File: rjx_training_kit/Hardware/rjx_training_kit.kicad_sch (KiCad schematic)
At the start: 20 parts, among them J1 Barrel_Jack_Switch, J2 Conn_01x32_Pin, J3 Conn_01x32_Pin, Q1 BC817, U1 TLV76133DCY, U2 LD39200DPUR

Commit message: [RJX]: Initial footprint assignment. This is subject to further review and analysis.
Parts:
- C1, C2, C3, C4: footprint (none) -> Capacitor_SMD:C_0603_1608Metric
- D1: footprint (none) -> LED_SMD:LED_0603_1608Metric
- H1, H2, H3, H4: footprint (none) -> MountingHole:MountingHole_3mm
- J1: footprint (none) -> Connector_BarrelJack:BarrelJack_Horizontal
- J2, J3: footprint (none) -> Connector_PinHeader_2.54mm:PinHeader_1x32_P2.54mm_Vertical
- R1, R2, R3, R4, R5: footprint (none) -> Resistor_SMD:R_0603_1608Metric
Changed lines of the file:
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@@
 			)
 		)
-		(property "Footprint" ""
+		(property "Footprint" "Resistor_SMD:R_0603_1608Metric"
 			(at 47.244 171.704 90)
 			(effects
@@
 			)
 		)
-		(property "Footprint" ""
+		(property "Footprint" "Capacitor_SMD:C_0603_1608Metric"
 			(at 132.3848 53.34 0)
 			(effects
@@
 			)
 		)
-		(property "Footprint" ""
+		(property "Footprint" "MountingHole:MountingHole_3mm"
 			(at 125.73 177.8 0)
 			(effects
@@
 			)
 		)
-		(property "Footprint" ""
+		(property "Footprint" "Connector_BarrelJack:BarrelJack_Horizontal"
 			(at 46.99 41.656 0)
 			(effects
@@
 			)
 		)
-		(property "Footprint" ""
+		(property "Footprint" "Resistor_SMD:R_0603_1608Metric"
 			(at 61.976 153.924 90)
 			(effects
@@
 			)
 		)
-		(property "Footprint" ""
+		(property "Footprint" "Capacitor_SMD:C_0603_1608Metric"
 			(at 35.8648 104.14 0)
 			(effects
@@
 			)
 		)
-		(property "Footprint" ""
+		(property "Footprint" "Connector_PinHeader_2.54mm:PinHeader_1x32_P2.54mm_Vertical"
 			(at 124.46 119.38 0)
 			(effects
@@
 			)
 		)
-		(property "Footprint" ""
+		(property "Footprint" "MountingHole:MountingHole_3mm"
 			(at 101.6 177.8 0)
 			(effects
@@
 			)
 		)
-		(property "Footprint" ""
+		(property "Footprint" "LED_SMD:LED_0603_1608Metric"
 			(at 60.96 162.56 0)
 			(effects
@@
 			)
 		)
-		(property "Footprint" ""
+		(property "Footprint" "Resistor_SMD:R_0603_1608Metric"
 			(at 41.656 158.496 90)
 			(effects
@@
 			)
 		)
-		(property "Footprint" ""
+		(property "Footprint" "Resistor_SMD:R_0603_1608Metric"
 			(at 144.526 32.766 90)
 			(effects
@@
 			)
 		)
-		(property "Footprint" ""
+		(property "Footprint" "Resistor_SMD:R_0603_1608Metric"
 			(at 144.526 49.276 90)
 			(effects
@@
 			)
 		)
-		(property "Footprint" ""
+		(property "Footprint" "MountingHole:MountingHole_3mm"
 			(at 125.73 185.42 0)
 			(effects
@@
 			)
 		)
-		(property "Footprint" ""
+		(property "Footprint" "Connector_PinHeader_2.54mm:PinHeader_1x32_P2.54mm_Vertical"
 			(at 106.68 119.38 0)
 			(effects
@@
 			)
 		)
-		(property "Footprint" ""
+		(property "Footprint" "MountingHole:MountingHole_3mm"
 			(at 101.6 185.42 0)
 			(effects
@@
 			)
 		)
-		(property "Footprint" ""
+		(property "Footprint" "Capacitor_SMD:C_0603_1608Metric"
 			(at 61.2648 104.14 0)
 			(effects
@@
 			)
 		)
-		(property "Footprint" ""
+		(property "Footprint" "Capacitor_SMD:C_0603_1608Metric"
 			(at 66.3448 54.61 0)
 			(effects

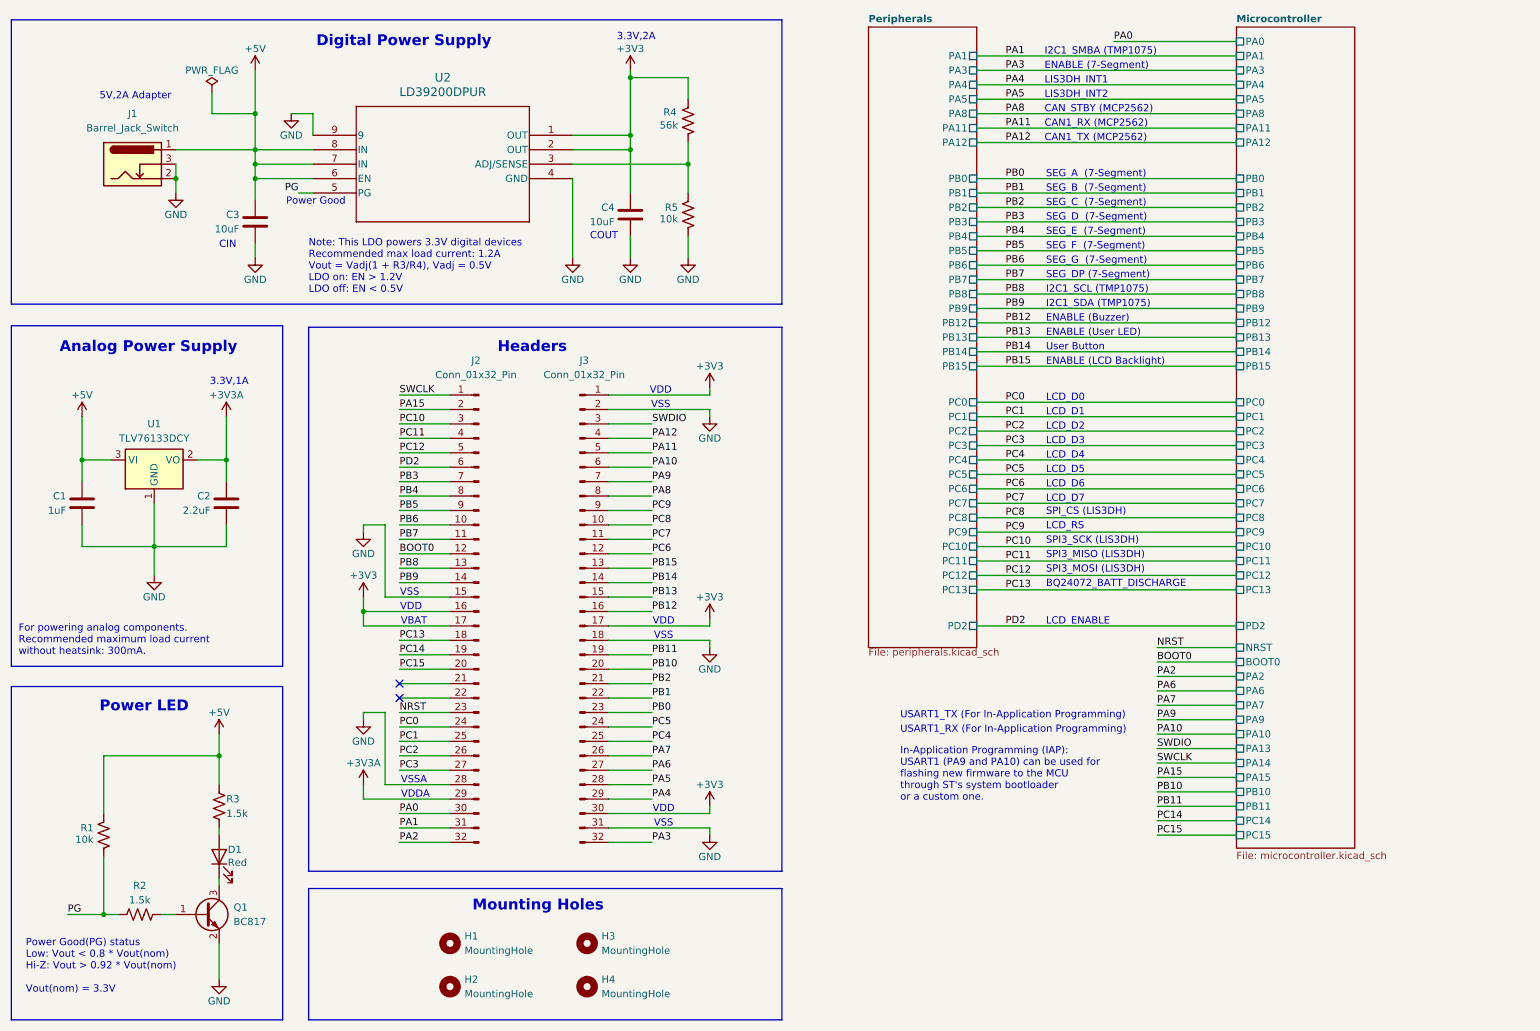
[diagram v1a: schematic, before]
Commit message: [RJX]: Schematic update with 3-pin SWD connector.
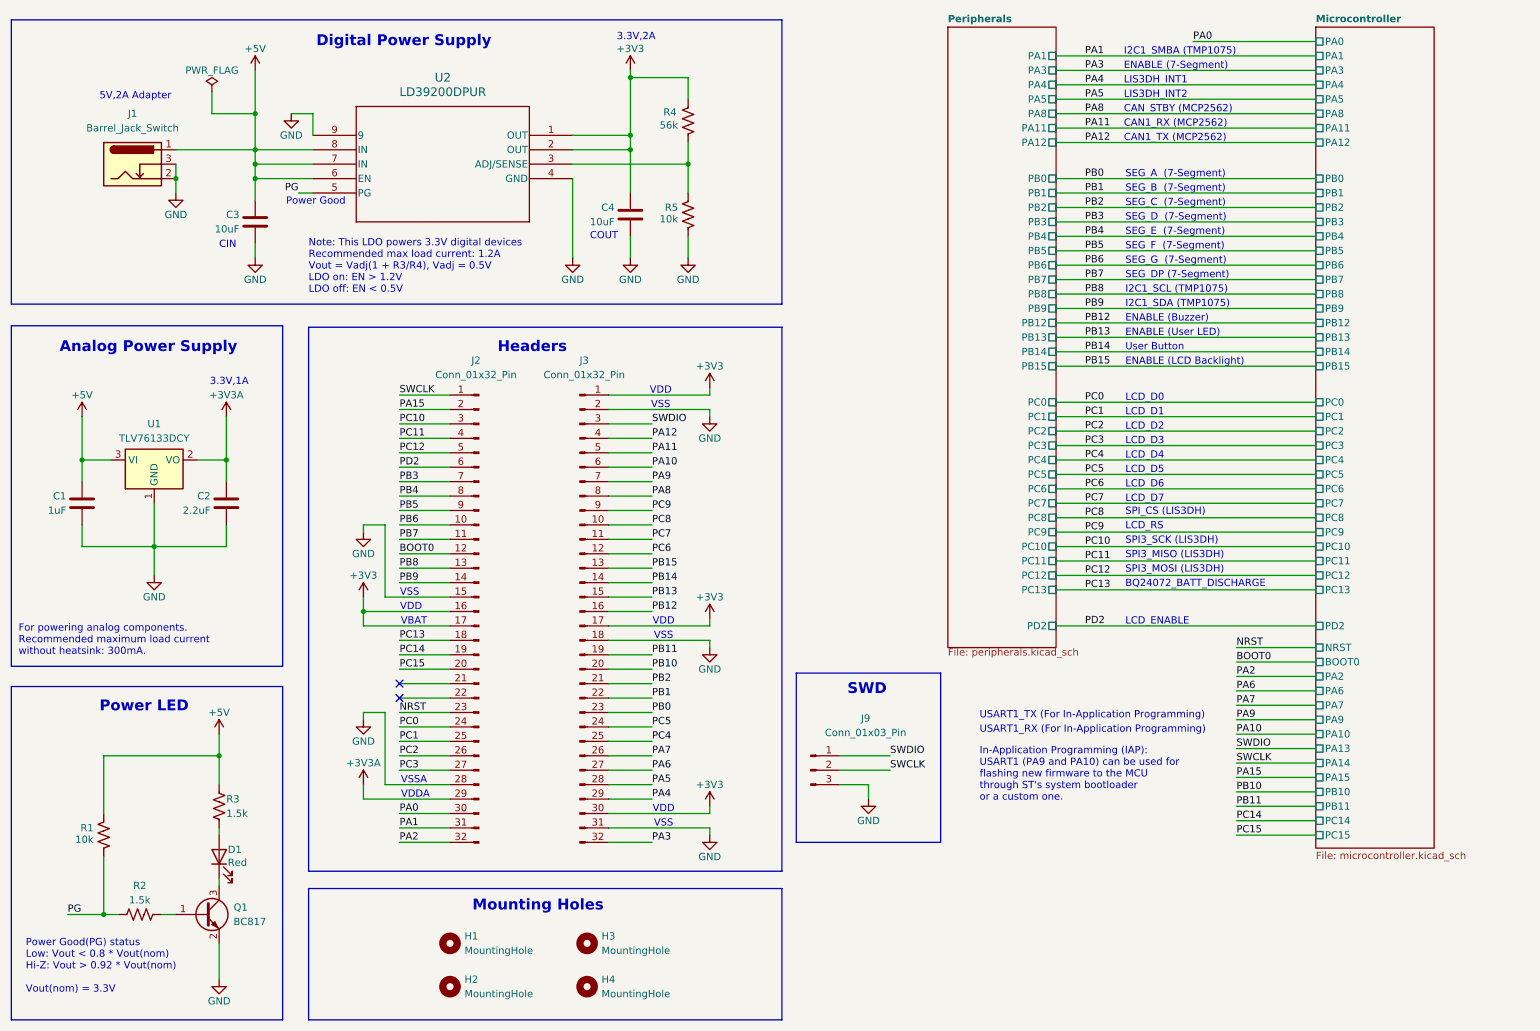
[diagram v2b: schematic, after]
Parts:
- added J9: Conn_01x03_Pin, Connector_PinHeader_2.54mm:PinHeader_1x03_P2.54mm_Horizontal, symbol Connector:Conn_01x03_Pin
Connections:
- net GND: now also J9.3 (Pin_3)
- net SWCLK: now also J9.2 (Pin_2)
- net SWDIO: now also J9.1 (Pin_1)
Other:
- note added: "SWD"
- company: (none) -> RJX Embedded
